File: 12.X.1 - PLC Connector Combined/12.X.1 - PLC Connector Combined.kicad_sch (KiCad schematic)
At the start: 0 parts

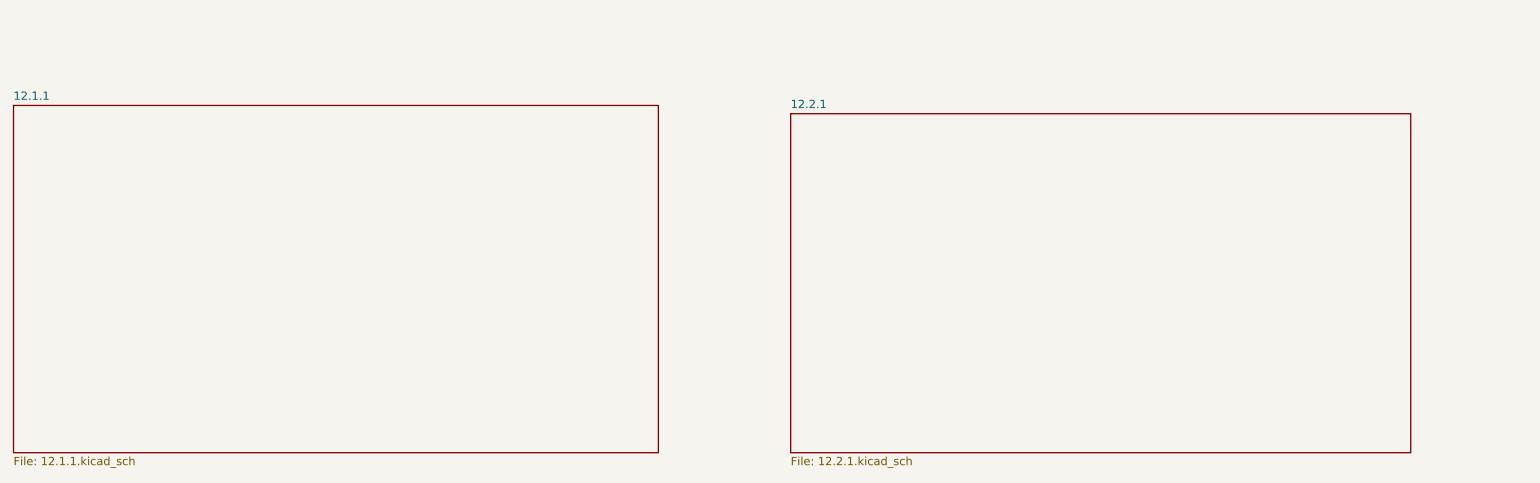
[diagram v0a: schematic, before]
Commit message: change pcb edge cuts
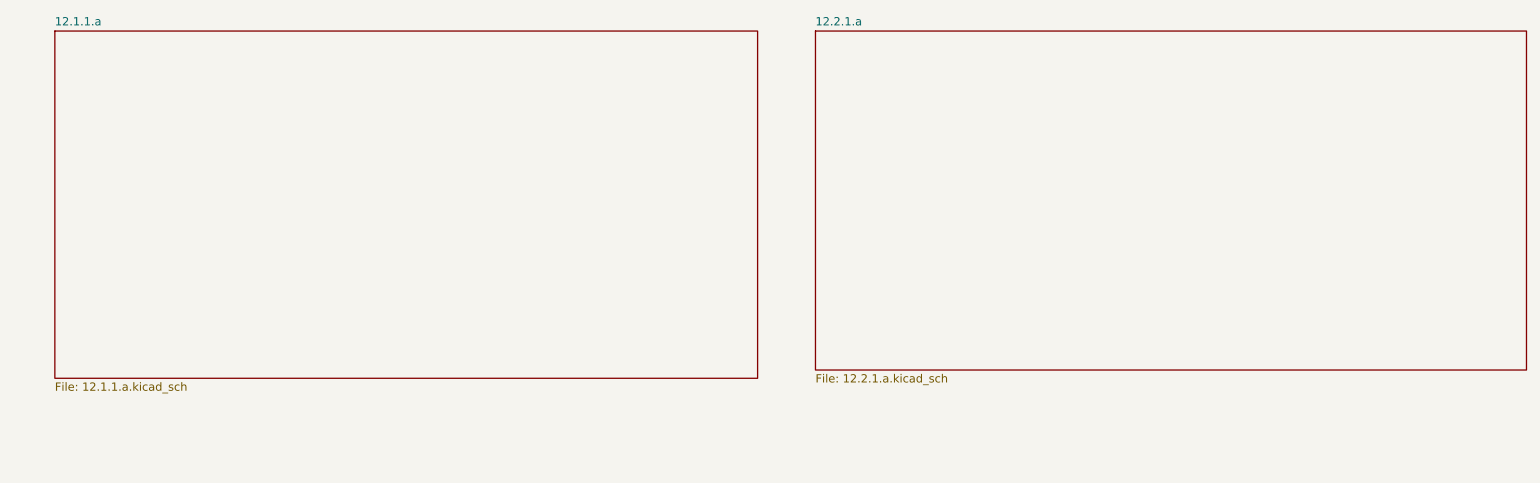
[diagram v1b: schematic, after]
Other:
- removed sheet 12.1.1
- removed sheet 12.2.1
- added sheet 12.1.1.a (12.1.1.a.kicad_sch)
- added sheet 12.2.1.a (12.2.1.a.kicad_sch)
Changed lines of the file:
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@@
 (kicad_sch (version 20230121) (generator eeschema)
   (paper "A4")
-  (sheet (at 33.02 69.85) (size 99.06 53.34) (fields_autoplaced)
+  (sheet (at 156.21 58.42) (size 109.22 52.07) (fields_autoplaced)
     (stroke (width 0.1524) (type solid))
     (fill (color 0 0 0 0.0000))
-    (property "Sheetname" "12.1.1" (at 33.02 69.1384 0)
+    (property "Sheetname" "12.2.1.a" (at 156.21 57.7084 0)
       (effects (font (size 1.27 1.27)) (justify left bottom))
     )
-    (property "Sheetfile" "12.1.1.kicad_sch" (at 33.02 123.7746 0)
+    (property "Sheetfile" "12.2.1.a.kicad_sch" (at 156.21 111.0746 0)
       (effects (font (size 1.27 1.27)) (justify left top))
     )
     (instances
       (project "12.X.1 - PLC Connector Combined"
-        (path "/0d1efd01-2b77-4213-8750-2a5840dff8e0" (page "3"))
+        (path "/e8fde896-61e0-40a5-97a7-fcbe64987e37" (page "3"))
       )
     )
   )
-  (sheet (at 152.4 71.12) (size 95.25 52.07) (fields_autoplaced)
+  (sheet (at 39.37 58.42) (size 107.95 53.34) (fields_autoplaced)
     (stroke (width 0.1524) (type solid))
     (fill (color 0 0 0 0.0000))
-    (property "Sheetname" "12.2.1" (at 152.4 70.4084 0)
+    (property "Sheetname" "12.1.1.a" (at 39.37 57.7084 0)
       (effects (font (size 1.27 1.27)) (justify left bottom))
     )
-    (property "Sheetfile" "12.2.1.kicad_sch" (at 152.4 123.7746 0)
+    (property "Sheetfile" "12.1.1.a.kicad_sch" (at 39.37 112.3446 0)
       (effects (font (size 1.27 1.27)) (justify left top))
     )
     (instances
       (project "12.X.1 - PLC Connector Combined"
-        (path "/0d1efd01-2b77-4213-8750-2a5840dff8e0" (page "3"))
+        (path "/e8fde896-61e0-40a5-97a7-fcbe64987e37" (page "2"))
       )
     )
